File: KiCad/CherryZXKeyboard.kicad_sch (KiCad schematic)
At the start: 100 parts, among them J1 Conn_01x05_Female, J2 Conn_01x08_Female, SW1 1, SW10 E, SW11 D, SW12 X, SW13 4, SW14 R, SW15 F, SW16 C, SW17 5, SW18 T, SW19 G, SW2 Q, SW20 V, SW21 6, SW22 Y, SW23 H, SW24 B, SW25 7, SW26 U, SW27 J, SW28 N, SW29 8, SW3 A, SW30 I, SW31 K, SW32 M, SW33 9, SW34 O, SW35 L, SW36 SYM, SW37 0, SW38 P, SW39 ENT, SW4 CAP, SW40 SPC, SW41 CAP, SW42 ;, SW43 ", SW44 ,, SW45 SYM, SW46 BREAK, SW47 EXTEND, SW48 DOT, SW49 LEFT, SW5 2, SW50 INV VID, SW51 TRUE VID, SW52 CAPS LOCK, SW53 EDIT, SW54 DOWN, SW55 UP, SW56 RIGHT, SW57 GRAPH, SW58 DEL, SW6 W, SW7 S, SW8 Z, SW9 3, U1 4066, U2 4066, U3 4066, U4 4066, U5 4066

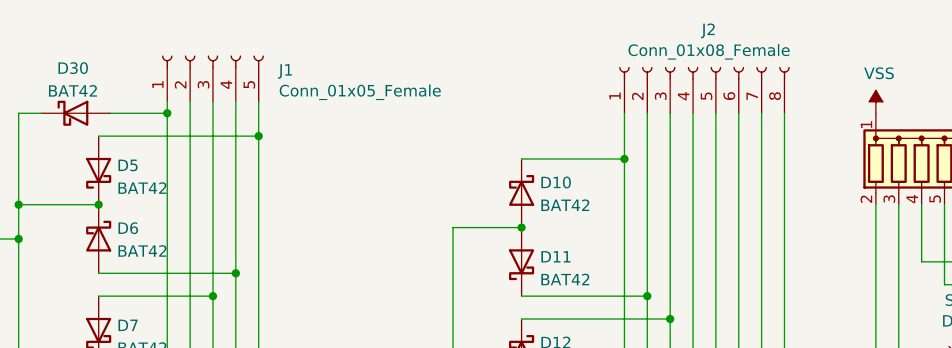
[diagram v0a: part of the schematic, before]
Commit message: Change footprints for keys 2U 6.25 U with mechanical stabilizers for PCB mounting
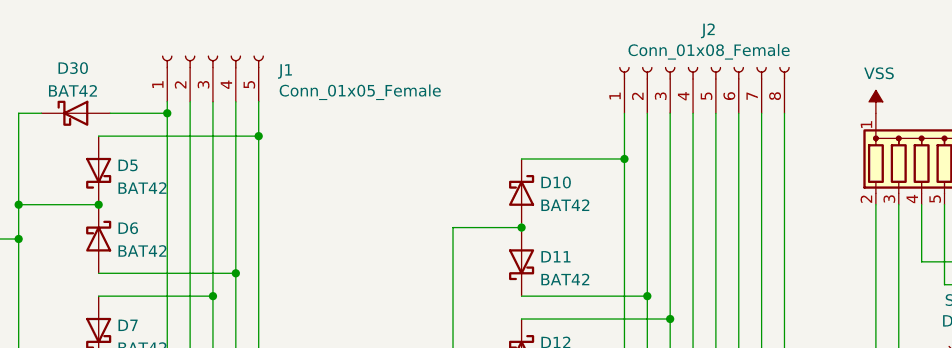
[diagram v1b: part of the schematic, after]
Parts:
- SW39, SW4, SW41, SW45: footprint Button_Switch_Keyboard:SW_Cherry_MX_1.00u_PCB -> Button_Switch_Keyboard:SW_Cherry_MX_2.00u_PCB
- SW40: footprint Button_Switch_Keyboard:SW_Cherry_MX_1.00u_PCB -> Button_Switch_Keyboard:SW_Cherry_MX_6.25u_PCB
